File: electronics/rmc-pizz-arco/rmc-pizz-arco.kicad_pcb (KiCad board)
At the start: 4 copper layers, 74.8 x 80.8 mm, 80 parts, among them J1 PZT, J2 PZT, J3 PZT, J4 PZT, J5 PZT, J6 PZT, J7 DIN-8, J8 PIZZ/ARCO, U1 OPA4191, U2 OPA4191, U3 OPA4191, U4 CD4066B, U5 CD4066B

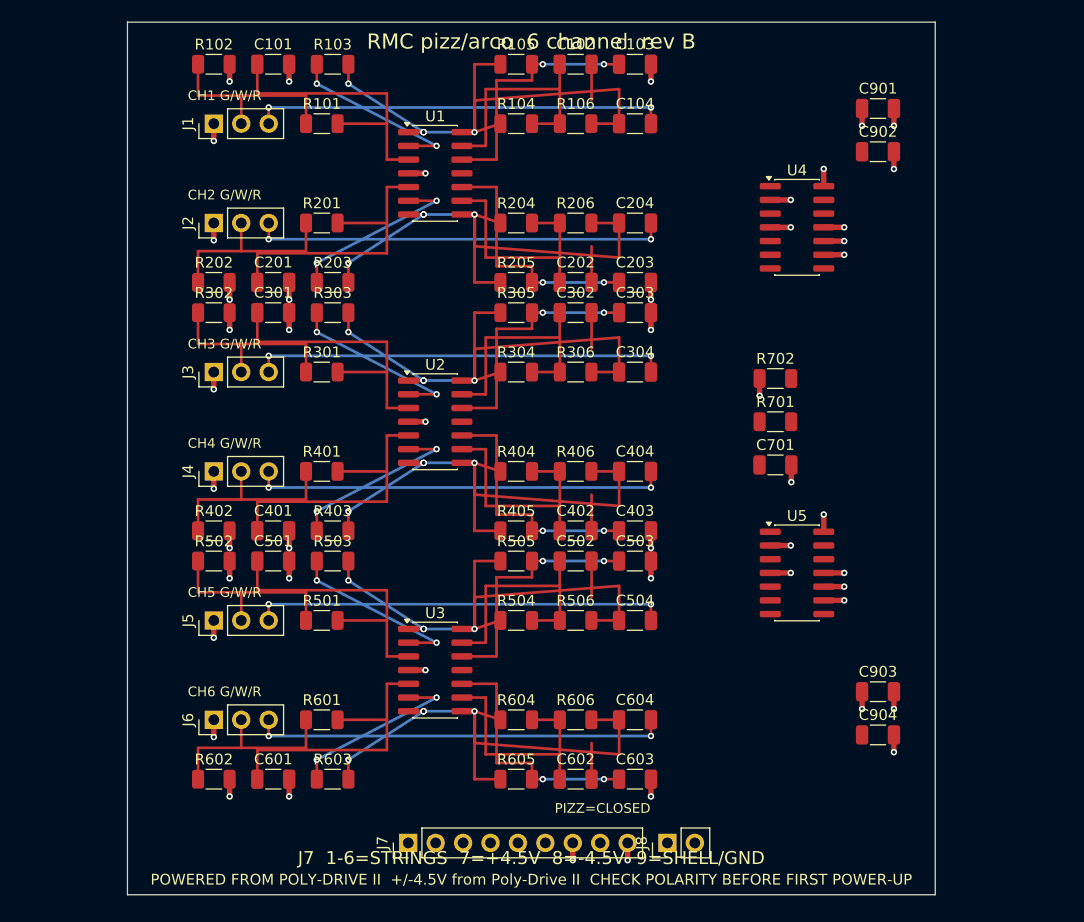
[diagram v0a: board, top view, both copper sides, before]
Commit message: Route the board to DRC-clean: 139 violations to zero
The routing is now entirely in gen_pcb.py; no autorouter is involved and
none is needed. 139 -> 34 -> 21 -> 18 -> 1 -> 0, with 0 unconnected items.
The full build passes: 53 nets and 233 pin connections matched against
design.py, 80 footprints linked, ERC clean, and the fab package writes.

Board measures 78.8 x 81.3 mm = 6406 mm2, against 88 x 112 = 9856 on main.

What the six-at-a-time faults turned out to be, since they are what the
rewrite is built around:

- Two structural rules decide every channel. The row line is the only place
  a net can change sides, so the crossings have to be shared out between the
  gaps in it -- and a 1206's own 1.8mm pad gap is where most of them go,
  which is the concrete payoff of RMC's advice about part size. And a net
  leaving the package deeper than another cannot turn towards the row inside
  the other's span; the three right-hand pins come out in exactly the wrong
  order for their targets, so APOUT gives way and makes its traverse on B.Cu.

- The old code had SWN crossing R04's pads outright, APOUT running as a
  diagonal across four lanes, and both buffer feedback nets crossing OUT's
  B.Cu spine. All three were systematic and each was worth six.

- R03 moves east of R01. Every gap in the row line west of R01.2 was already
  spoken for, and R03's own two pads are the crossings the buffer needs.

- Plane stub offsets are now chosen from the channel's sign, so both halves
  of a block are mirrored. They were not, and the fault appeared on exactly
  half the board.

Board-level nets get a function of their own. OUT and SWN fill B.Cu and F.Cu
respectively for most of the board's height, so V-, SW_CTL and SW_TOG cannot
use the corridor at all; they run down the strip east of the switches and
reach the tail connectors from above.

The right-hand column moves out 2mm and the header down 0.5mm, both to make
room measured rather than guessed: the fan-in above J7 needs six rows th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
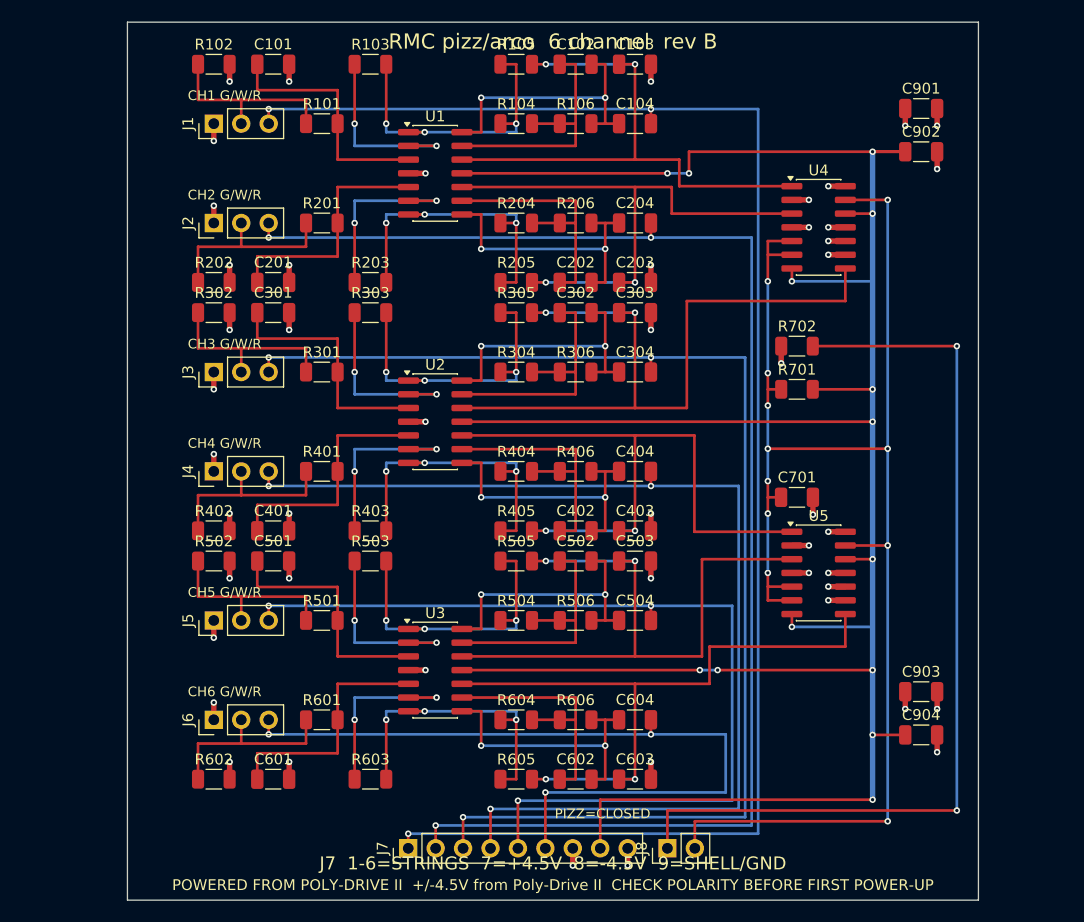
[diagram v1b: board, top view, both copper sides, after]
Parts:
- moved C901 4.00 mm to (73.5, 8.00)
- moved C902 4.00 mm to (73.5, 12.0)
- moved C903 4.00 mm to (73.5, 62.0)
- moved C904 4.00 mm to (73.5, 66.0)
- moved C701 3.61 mm to (62.0, 44.0)
- moved R701 3.61 mm to (62.0, 34.0)
- moved R702 3.61 mm to (62.0, 30.0)
- moved R103 3.50 mm to (22.5, 3.90)
- moved R203 3.50 mm to (22.5, 24.1)
- moved R303 3.50 mm to (22.5, 26.9)
- moved R403 3.50 mm to (22.5, 47.1)
- moved R503 3.50 mm to (22.5, 49.9)
- moved R603 3.50 mm to (22.5, 70.1)
- moved U4 2.00 mm to (64.0, 19.0)
- moved U5 2.00 mm to (64.0, 51.0)
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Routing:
- net V-: track 0.00 -> 242.8 mm, vias 0 -> 14
- net SW_CTL: track 0.00 -> 141.5 mm, vias 0 -> 11
- net OUT1: track 38.4 -> 148.9 mm, vias 2 -> 3
- net OUT2: track 38.4 -> 133.2 mm, vias 2 -> 3
- net SW_TOG: track 0.00 -> 86.6 mm, vias 0 -> 2
- net OUT3: track 38.4 -> 118.4 mm, vias 2 -> 3
- net OUT4: track 38.4 -> 102.8 mm, vias 2 -> 3
- net OUT5: track 38.4 -> 87.9 mm, vias 2 -> 3
- net SWN3: track 23.4 -> 68.3 mm
- net SWN6: track 23.4 -> 61.8 mm
- net SWN5: track 23.4 -> 59.4 mm
- net SWN4: track 23.4 -> 59.3 mm
- net OUT6: track 38.4 -> 72.3 mm, vias 2 -> 3
- net SWN1: track 23.4 -> 52.9 mm
- net SWN2: track 23.4 -> 52.9 mm
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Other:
- board size 74.8 x 80.8 mm -> 78.8 x 81.3 mm
